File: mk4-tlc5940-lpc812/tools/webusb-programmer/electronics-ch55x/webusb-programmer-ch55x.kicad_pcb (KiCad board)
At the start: 2 copper layers, 38 x 20 mm, 19 parts, among them J1 USB_B_Micro, J2 Light Controller, Q1 PMV30UN, U1 CH552G, U3 STMPS2141STR

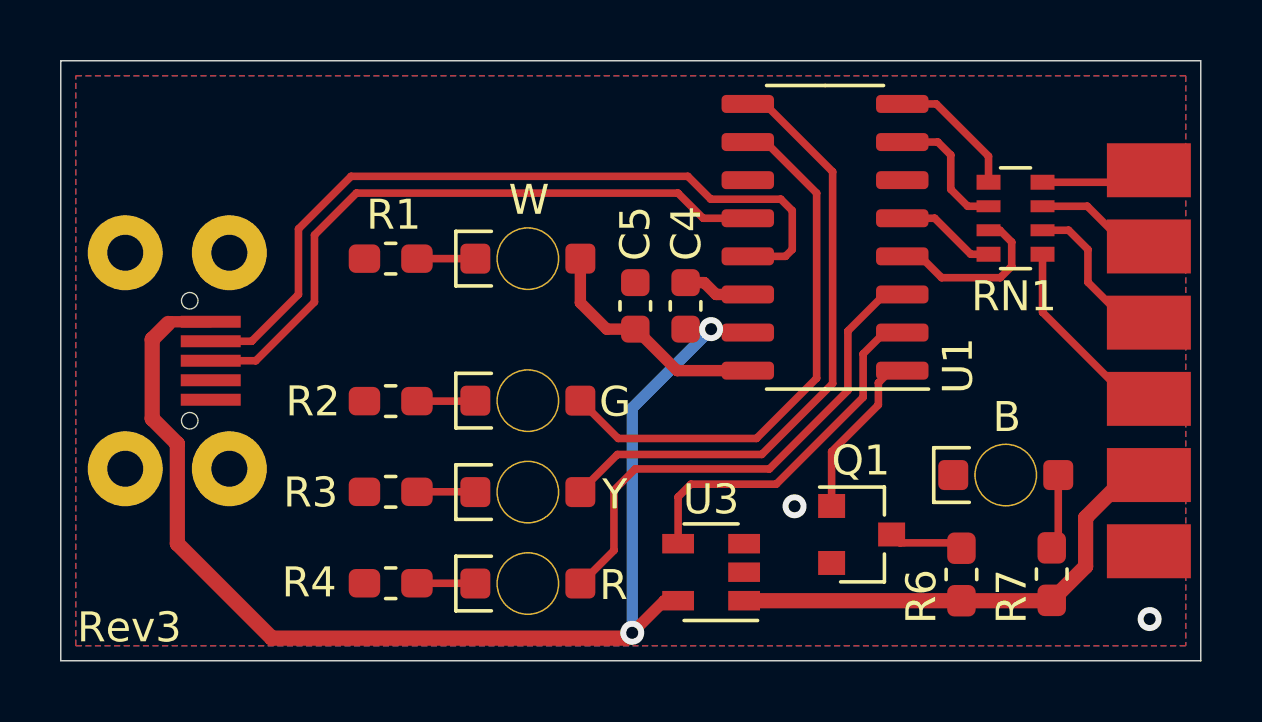
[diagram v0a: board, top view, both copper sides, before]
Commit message: Reverse LED polarity to prevent pull-up from lighting them up
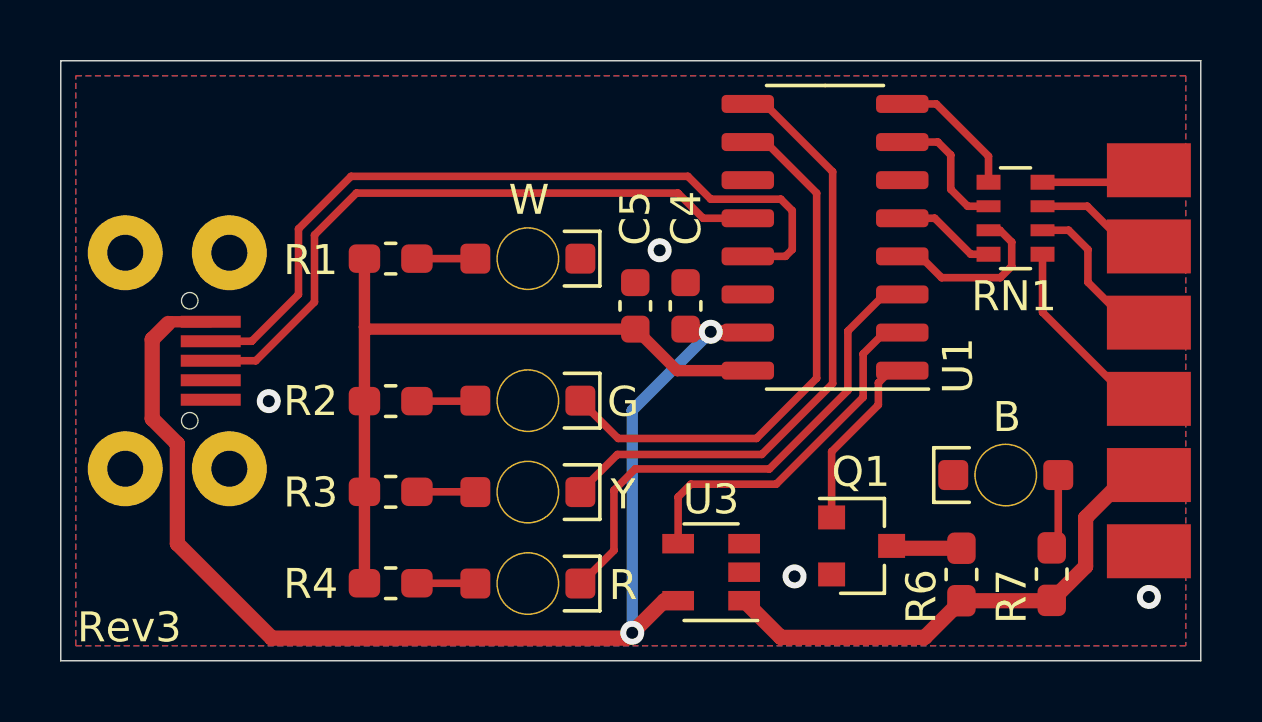
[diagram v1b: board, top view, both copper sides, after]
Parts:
- moved Q1 0.38 mm to (126.7, 106.2)
- turned D1 to 180 degrees
- turned D2 to 180 degrees
- turned D3 to 180 degrees
- turned D4 to 180 degrees
- turned R1 to 0 degrees
- turned R2 to 0 degrees
- turned R3 to 0 degrees
- turned R4 to 0 degrees
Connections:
- D1 pad 1: Net-(D1-Pad1) -> GND
- D1 pad 2: +3V3 -> Net-(D1-Pad2)
- D2 pad 1: Net-(D2-Pad1) -> /OK
- D2 pad 2: /OK -> Net-(D2-Pad2)
- D3 pad 1: Net-(D3-Pad1) -> /BUSY
- D3 pad 2: /BUSY -> Net-(D3-Pad2)
- D4 pad 1: Net-(D4-Pad1) -> /ERROR
- D4 pad 2: /ERROR -> Net-(D4-Pad2)
- R1 pad 1: Net-(D1-Pad1) -> +3V3
- R1 pad 2: GND -> Net-(D1-Pad2)
- R2 pad 1: Net-(D2-Pad1) -> +3V3
- R2 pad 2: GND -> Net-(D2-Pad2)
- R3 pad 1: Net-(D3-Pad1) -> +3V3
- R3 pad 2: GND -> Net-(D3-Pad2)
- R4 pad 1: Net-(D4-Pad1) -> +3V3
- R4 pad 2: GND -> Net-(D4-Pad2)
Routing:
- net +3V3: track 7.99 -> 24.2 mm
- net GND: track 2.24 -> 0.00 mm, vias 2 -> 4
- net Net-(D2-Pad2): track 0.00 -> 1.95 mm
- net Net-(D2-Pad1): track 1.95 -> 0.00 mm
- net Net-(D4-Pad2): track 0.00 -> 1.95 mm
- net Net-(D4-Pad1): track 1.95 -> 0.00 mm
- net Net-(D3-Pad2): track 0.00 -> 1.95 mm
- net Net-(D3-Pad1): track 1.95 -> 0.00 mm
- net Net-(D1-Pad2): track 0.00 -> 1.95 mm
- net Net-(D1-Pad1): track 1.95 -> 0.00 mm
- net /VLIGHT: track 16.2 -> 17.2 mm
